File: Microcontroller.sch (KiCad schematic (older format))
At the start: 17 parts

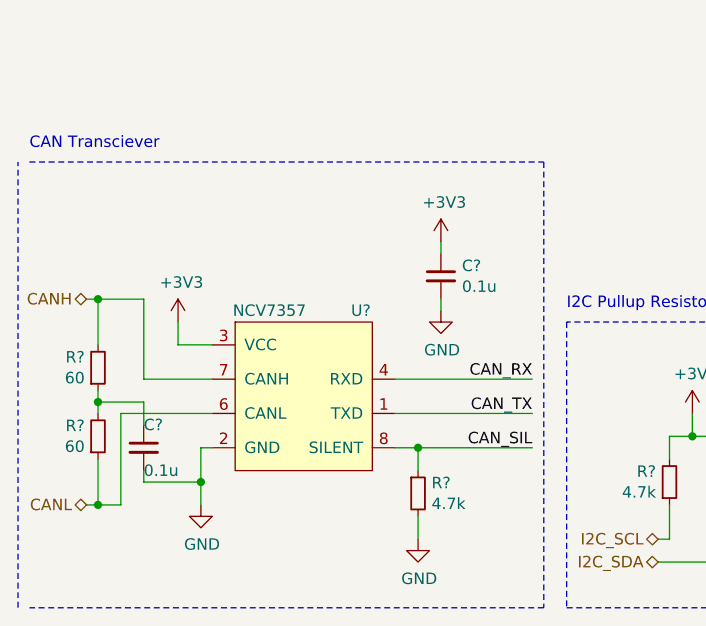
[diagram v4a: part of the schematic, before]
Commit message: Added current sense
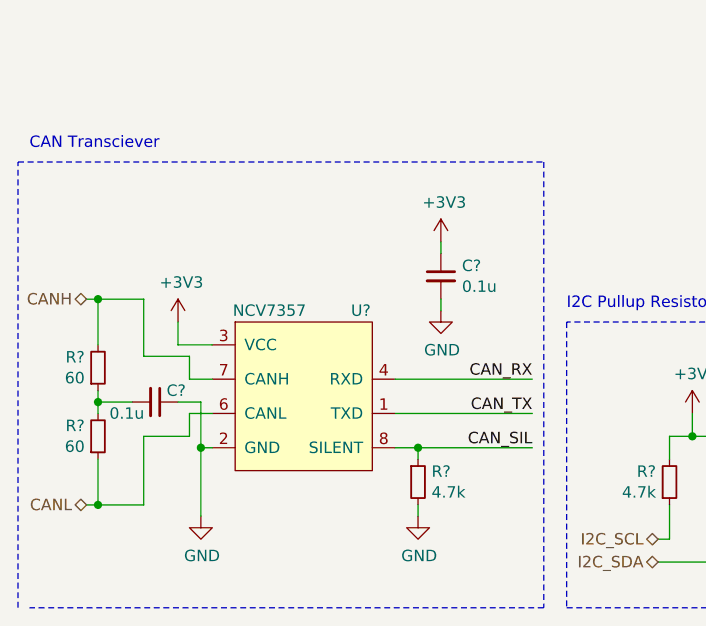
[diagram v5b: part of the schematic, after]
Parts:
- removed C?: 0.1u, Capacitor_SMD:C_0603_1608Metric, symbol Device:C_Small
- added C?: 0.1u, Capacitor_SMD:C_0603_1608Metric, symbol Device:C_Small
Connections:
- net GND: now also C?.1
- net at R?.1, R?.2: now also C?.2
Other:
- moved on the sheet: R?
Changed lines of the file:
@@
 L Device:R_Small R?
 U 1 1 5F6FEA9A
-P 2250 7200
-F 0 "R?" H 2309 7246 50  0000 L CNN
-F 1 "4.7k" H 2309 7155 50  0000 L CNN
-F 2 "" H 2250 7200 50  0001 C CNN
-F 3 "~" H 2250 7200 50  0001 C CNN
-	1    2250 7200
+P 2250 7150
+F 0 "R?" H 2309 7196 50  0000 L CNN
+F 1 "4.7k" H 2309 7105 50  0000 L CNN
+F 2 "" H 2250 7150 50  0001 C CNN
+F 3 "~" H 2250 7150 50  0001 C CNN
+	1    2250 7150
 	1    0    0    -1
 $EndComp
 Wire Wire Line
-	2250 7100 2250 7000
+	2250 7050 2250 7000
 Connection ~ 2250 7000
 Wire Wire Line
 	2250 7000 2750 7000
 Wire Wire Line
-	2250 7300 2250 7400
+	2250 7250 2250 7300
 $Comp
 L power:GND #PWR?
 U 1 1 5F702399
-P 2250 7400
-F 0 "#PWR?" H 2250 7150 50  0001 C CNN
-F 1 "GND" H 2255 7227 50  0000 C CNN
-F 2 "" H 2250 7400 50  0001 C CNN
-F 3 "" H 2250 7400 50  0001 C CNN
-	1    2250 7400
+P 2250 7300
+F 0 "#PWR?" H 2250 7050 50  0001 C CNN
+F 1 "GND" H 2255 7127 50  0000 C CNN
+F 2 "" H 2250 7300 50  0001 C CNN
+F 3 "" H 2250 7300 50  0001 C CNN
+	1    2250 7300
 	1    0    0    -1
 $EndComp
@@
 Wire Notes Line
 	500  7700 500  5750
-Wire Notes Line
-	550  5750 2800 5750
 Wire Notes Line
 	2800 5750 2800 7700
@@
 	1350 7000 1300 7000
 Wire Wire Line
-	1050 6800 850  6800
-Wire Wire Line
-	850  6800 850  6750
-Wire Wire Line
-	850  6800 850  6850
-Connection ~ 850  6800
-Wire Wire Line
 	800  6350 850  6350
 Wire Wire Line
@@
 Text HLabel 800  6350 0    50   BiDi ~ 0
 CANH
-Wire Wire Line
-	1050 6900 1050 6800
 $Comp
-L Device:C_Small C?
-U 1 1 5F7517A6
-P 1050 7000
-F 0 "C?" H 1050 7100 50  0000 L CNN
-F 1 "0.1u" H 1050 6900 50  0000 L CNN
-F 2 "Capacitor_SMD:C_0603_1608Metric" H 1050 7000 50  0001 C CNN
-F 3 "~" H 1050 7000 50  0001 C CNN
-	1    1050 7000
+L power:GND #PWR?
+U 1 1 5F6C9398
+P 1300 7300
+F 0 "#PWR?" H 1300 7050 50  0001 C CNN
+F 1 "GND" H 1305 7127 50  0000 C CNN
+F 2 "" H 1300 7300 50  0001 C CNN
+F 3 "" H 1300 7300 50  0001 C CNN
+	1    1300 7300
 	1    0    0    -1
 $EndComp
 Wire Wire Line
-	1050 7150 1050 7100
+	850  6350 1050 6350
+Wire Wire Line
+	1050 6350 1050 6600
+Connection ~ 850  6350
+Connection ~ 850  7250
+Wire Notes Line
+	500  5750 2800 5750
+Wire Wire Line
+	1300 7000 1300 7300
+Wire Wire Line
+	850  6750 850  6800
+Wire Wire Line
+	850  6800 1000 6800
+Connection ~ 850  6800
+Wire Wire Line
+	850  6800 850  6850
 $Comp
-L power:GND #PWR?
-U 1 1 5F6C9398
-P 1300 7250
-F 0 "#PWR?" H 1300 7000 50  0001 C CNN
-F 1 "GND" H 1305 7077 50  0000 C CNN
-F 2 "" H 1300 7250 50  0001 C CNN
-F 3 "" H 1300 7250 50  0001 C CNN
-	1    1300 7250
-	1    0    0    -1
+L Device:C_Small C?
+U 1 1 5F7B3B2F
+P 1100 6800
+F 0 "C?" V 1050 6850 50  0000 L CNN
+F 1 "0.1u" V 1150 6600 50  0000 L CNN
+F 2 "Capacitor_SMD:C_0603_1608Metric" H 1100 6800 50  0001 C CNN
+F 3 "~" H 1100 6800 50  0001 C CNN
+	1    1100 6800
+	0    1    1    0
 $EndComp
 Wire Wire Line
-	1300 7250 1300 7150
+	1200 6800 1300 6800
 Wire Wire Line
-	1300 7000 1300 7150
-Connection ~ 1300 7150
+	1300 6800 1300 7000
+Connection ~ 1300 7000
 Wire Wire Line
-	1050 7150 1300 7150
+	1350 6700 1250 6700
 Wire Wire Line
-	850  6350 1050 6350
+	1250 6700 1250 6600
 Wire Wire Line
-	1050 6350 1050 6700
+	1050 6600 1250 6600
 Wire Wire Line
-	1050 6700 1350 6700
-Connection ~ 850  6350
+	1350 6850 1250 6850
 Wire Wire Line
-	850  7250 950  7250
-Connection ~ 850  7250
+	1250 6850 1250 6950
 Wire Wire Line
-	950  7250 950  6850
+	1250 6950 1050 6950
 Wire Wire Line
-	950  6850 1350 6850
+	1050 6950 1050 7250
+Wire Wire Line
+	850  7250 1050 7250
 $EndSCHEMATC

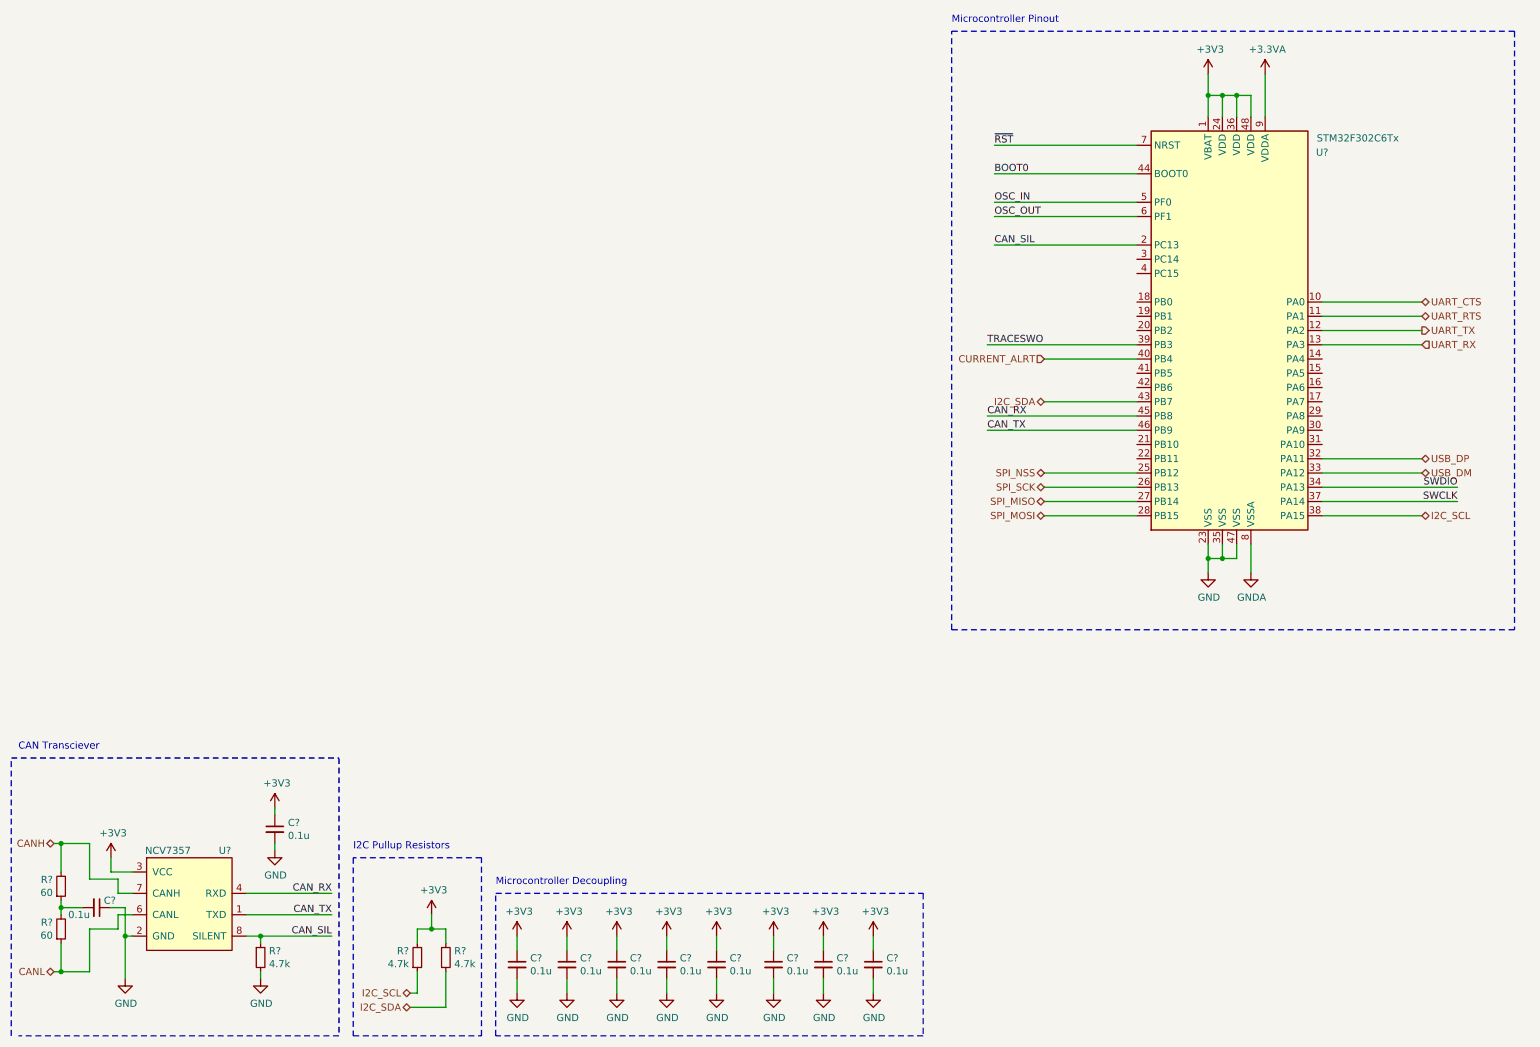
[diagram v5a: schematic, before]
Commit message: Added external oscillator
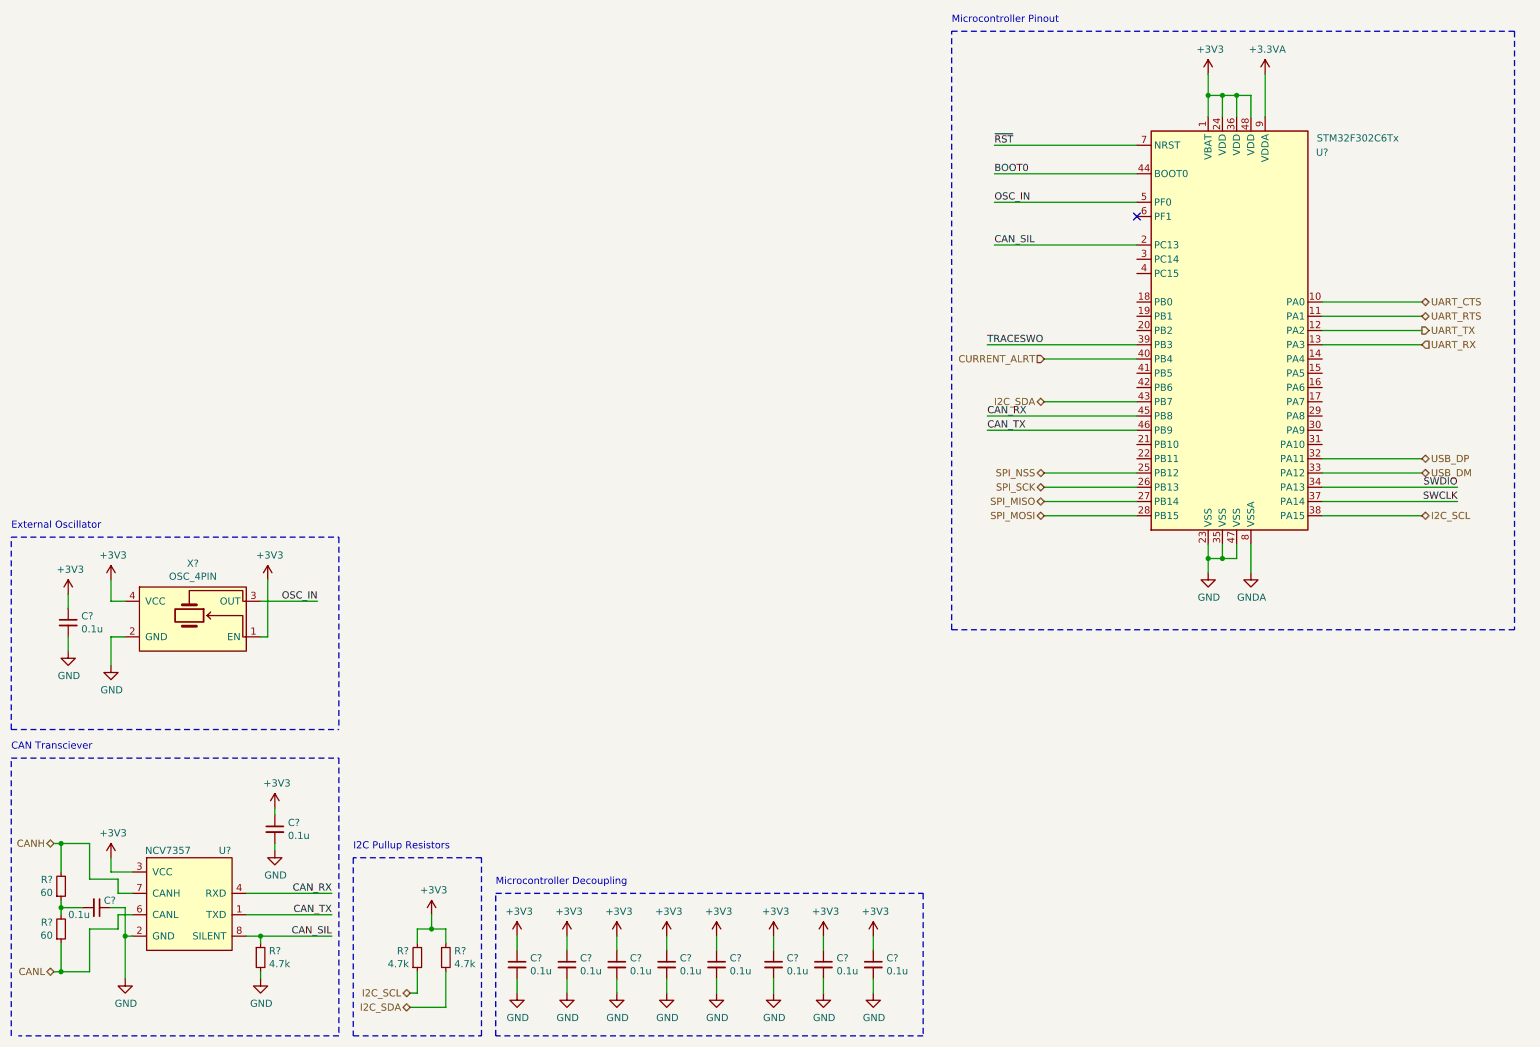
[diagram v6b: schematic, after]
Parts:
- added C?: 0.1u, Capacitor_SMD:C_0603_1608Metric, symbol Device:C_Small
- added X?: OSC_4PIN, symbol ReflowOven:OSC_4PIN
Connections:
- net +3V3: now also C?.1, X?.1 (EN), X?.4 (VCC)
- net GND: now also C?.2, X?.2 (GND)
- net OSC_IN: now also X?.3 (OUT)
- net OSC_OUT: no longer names the net of U?.6 (PF1)
- no-connect marks 0 -> 1
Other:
- note added: "External Oscillator"
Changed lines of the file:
@@
 OSC_IN
-Wire Wire Line
-	8400 1950 7400 1950
-Text Label 7400 1950 0    50   ~ 0
-OSC_OUT
 Wire Wire Line
 	8400 1650 7400 1650
@@
 Wire Notes Line
 	2800 5750 2800 7700
-Text Notes 550  5700 0    50   ~ 0
+Text Notes 500  5700 0    50   ~ 0
 CAN Transciever
 Text HLabel 3300 7400 0    50   BiDi ~ 0
@@
 Wire Wire Line
 	850  7250 1050 7250
+$Comp
+L ReflowOven:OSC_4PIN X?
+U 1 1 5F7EB02C
+P 1800 4750
+F 0 "X?" H 1775 5115 50  0000 C CNN
+F 1 "OSC_4PIN" H 1775 5024 50  0000 C CNN
+F 2 "" V 1750 4750 50  0001 C CNN
+F 3 "" V 1750 4750 50  0001 C CNN
+	1    1800 4750
+	1    0    0    -1
+$EndComp
+Wire Wire Line
+	2250 4650 2650 4650
+Text Label 2650 4650 2    50   ~ 0
+OSC_IN
+Wire Wire Line
+	2250 4900 2300 4900
+Wire Wire Line
+	2300 4900 2300 4500
+$Comp
+L power:+3V3 #PWR?
+U 1 1 5F7F8C2F
+P 2300 4500
+F 0 "#PWR?" H 2300 4350 50  0001 C CNN
+F 1 "+3V3" H 2315 4673 50  0000 C CNN
+F 2 "" H 2300 4500 50  0001 C CNN
+F 3 "" H 2300 4500 50  0001 C CNN
+	1    2300 4500
+	1    0    0    -1
+$EndComp
+Wire Wire Line
+	1300 4650 1200 4650
+Wire Wire Line
+	1200 4650 1200 4500
+$Comp
+L power:+3V3 #PWR?
+U 1 1 5F803440
+P 1200 4500
+F 0 "#PWR?" H 1200 4350 50  0001 C CNN
+F 1 "+3V3" H 1215 4673 50  0000 C CNN
+F 2 "" H 1200 4500 50  0001 C CNN
+F 3 "" H 1200 4500 50  0001 C CNN
+	1    1200 4500
+	1    0    0    -1
+$EndComp
+Wire Wire Line
+	1300 4900 1200 4900
+Wire Wire Line
+	1200 4900 1200 5100
+$Comp
+L power:GND #PWR?
+U 1 1 5F80755B
+P 1200 5100
+F 0 "#PWR?" H 1200 4850 50  0001 C CNN
+F 1 "GND" H 1205 4927 50  0000 C CNN
+F 2 "" H 1200 5100 50  0001 C CNN
+F 3 "" H 1200 5100 50  0001 C CNN
+	1    1200 5100
+	1    0    0    -1
+$EndComp
+$Comp
+L power:+3V3 #PWR?
+U 1 1 5F809223
+P 900 4600
+F 0 "#PWR?" H 900 4450 50  0001 C CNN
+F 1 "+3V3" H 915 4773 50  0000 C CNN
+F 2 "" H 900 4600 50  0001 C CNN
+F 3 "" H 900 4600 50  0001 C CNN
+	1    900  4600
+	1    0    0    -1
+$EndComp
+$Comp
+L Device:C_Small C?
+U 1 1 5F809229
+P 900 4800
+F 0 "C?" H 992 4846 50  0000 L CNN
+F 1 "0.1u" H 992 4755 50  0000 L CNN
+F 2 "Capacitor_SMD:C_0603_1608Metric" H 900 4800 50  0001 C CNN
+F 3 "~" H 900 4800 50  0001 C CNN
+	1    900  4800
+	1    0    0    -1
+$EndComp
+$Comp
+L power:GND #PWR?
+U 1 1 5F80922F
+P 900 5000
+F 0 "#PWR?" H 900 4750 50  0001 C CNN
+F 1 "GND" H 905 4827 50  0000 C CNN
+F 2 "" H 900 5000 50  0001 C CNN
+F 3 "" H 900 5000 50  0001 C CNN
+	1    900  5000
+	1    0    0    -1
+$EndComp
+Wire Wire Line
+	900  5000 900  4900
+Wire Wire Line
+	900  4700 900  4600
+Wire Notes Line
+	500  5550 500  4200
+Wire Notes Line
+	2800 4200 2800 5550
+Wire Notes Line
+	500  5550 2800 5550
+Text Notes 500  4150 0    50   ~ 0
+External Oscillator
+Wire Notes Line
+	500  4200 2800 4200
+NoConn ~ 8400 1950
 $EndSCHEMATC

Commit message: Preliminary Microcontroller schematic done
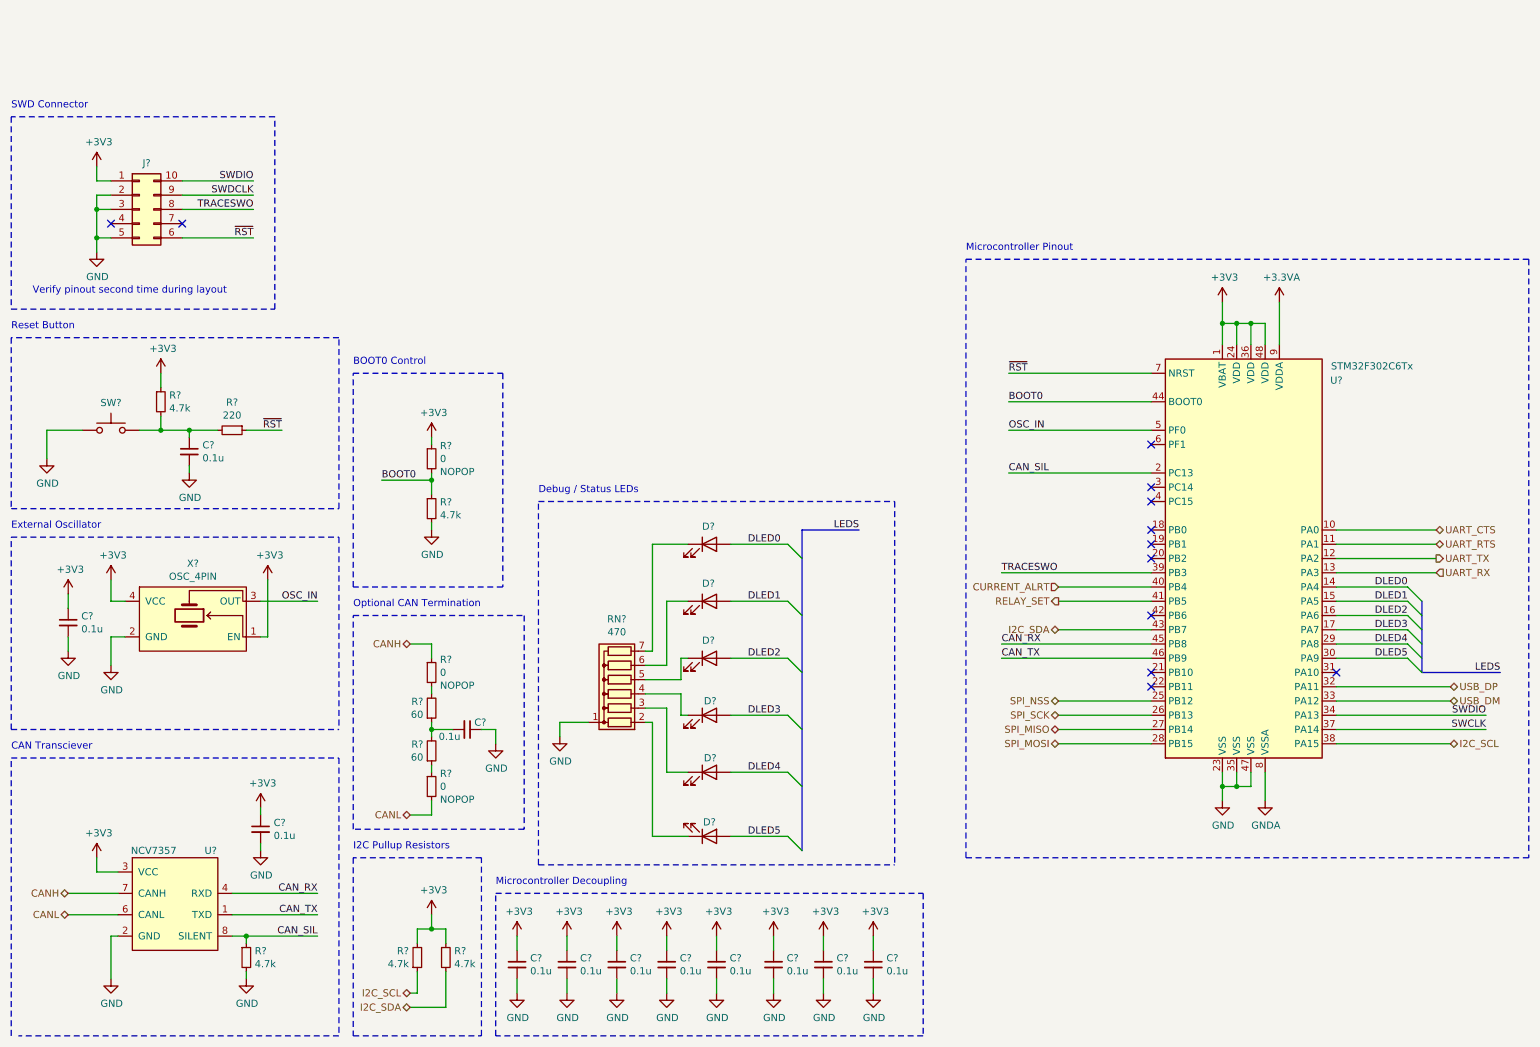
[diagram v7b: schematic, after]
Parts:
- added C?: 0.1u, Capacitor_SMD:C_0603_1608Metric, symbol Device:C_Small
- added D? (x6): LED, symbol Device:LED
- added J?: Conn_02x05_Counter_Clockwise, symbol Connector_Generic:Conn_02x05_Counter_Clockwise
- added R? (x2): 4.7k, symbol Device:R_Small
- added R?: 220, symbol Device:R_Small
- added R? (x3): 0, symbol Device:R_Small
- added RN?: 470, Resistor_THT:R_Array_SIP7, symbol Device:R_Network06
- added SW?: SW_Push, symbol Switch:SW_Push
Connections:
- net +3V3: now also J?.1 (Pin_1), R?.1, R?.1
- net BOOT0: now also R?.1, R?.2
- net CANH: now also R?.1; no longer R?.2
- net CANL: now also R?.2; no longer R?.1
- net GND: now also C?.2, J?.2 (Pin_2), J?.3 (Pin_3), J?.5 (Pin_5), R?.2, RN?.1 (common), SW?.1
- net SWDIO: now also J?.10 (Pin_10)
- net TRACESWO: now also J?.8 (Pin_8)
- net ~RST: now also J?.6 (Pin_6), R?.1
- net DLED0: now reaches U?.14 (PA4)
- net DLED0: now also D?.2 (A)
- net DLED1: now reaches U?.15 (PA5)
- net DLED1: now also D?.2 (A)
- net DLED2: now reaches U?.16 (PA6)
- net DLED2: now also D?.2 (A)
- net DLED3: now reaches U?.17 (PA7)
- net DLED3: now also D?.2 (A)
- net DLED4: now reaches U?.29 (PA8)
- net DLED4: now also D?.2 (A)
- net DLED5: now reaches U?.30 (PA9)
- net DLED5: now also D?.2 (A)
- net RELAY_SET: now reaches U?.41 (PB5)
- new net: R?.2, R?.2
- new net: R?.1, R?.1
- new net: D?.1 (K), RN?.4 (R3)
- new net: D?.1 (K), RN?.5 (R4)
- new net: D?.1 (K), RN?.6 (R5)
- new net: D?.1 (K), RN?.7 (R6)
- new net: C?.1, R?.2, R?.2, SW?.2
- new net: D?.1 (K), RN?.2 (R1)
- new net: D?.1 (K), RN?.3 (R2)
- new net SWDCLK: J?.9 (Pin_9)
- no-connect marks 1 -> 12
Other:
- note added: "BOOT0 Control"
- note added: "Debug / Status LEDs"
- note added: "Optional CAN Termination"
- note added: "Reset Button"
- note added: "SWD Connector"
- note added: "Verify pinout second time during layout"
- moved on the sheet: C?, R?, U?
